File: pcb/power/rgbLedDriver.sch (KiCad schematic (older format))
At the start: 39 parts, among them Q1 Q_NPN_BCE, Q2 Q_NPN_BCE, Q3 Q_PMOS_DGS

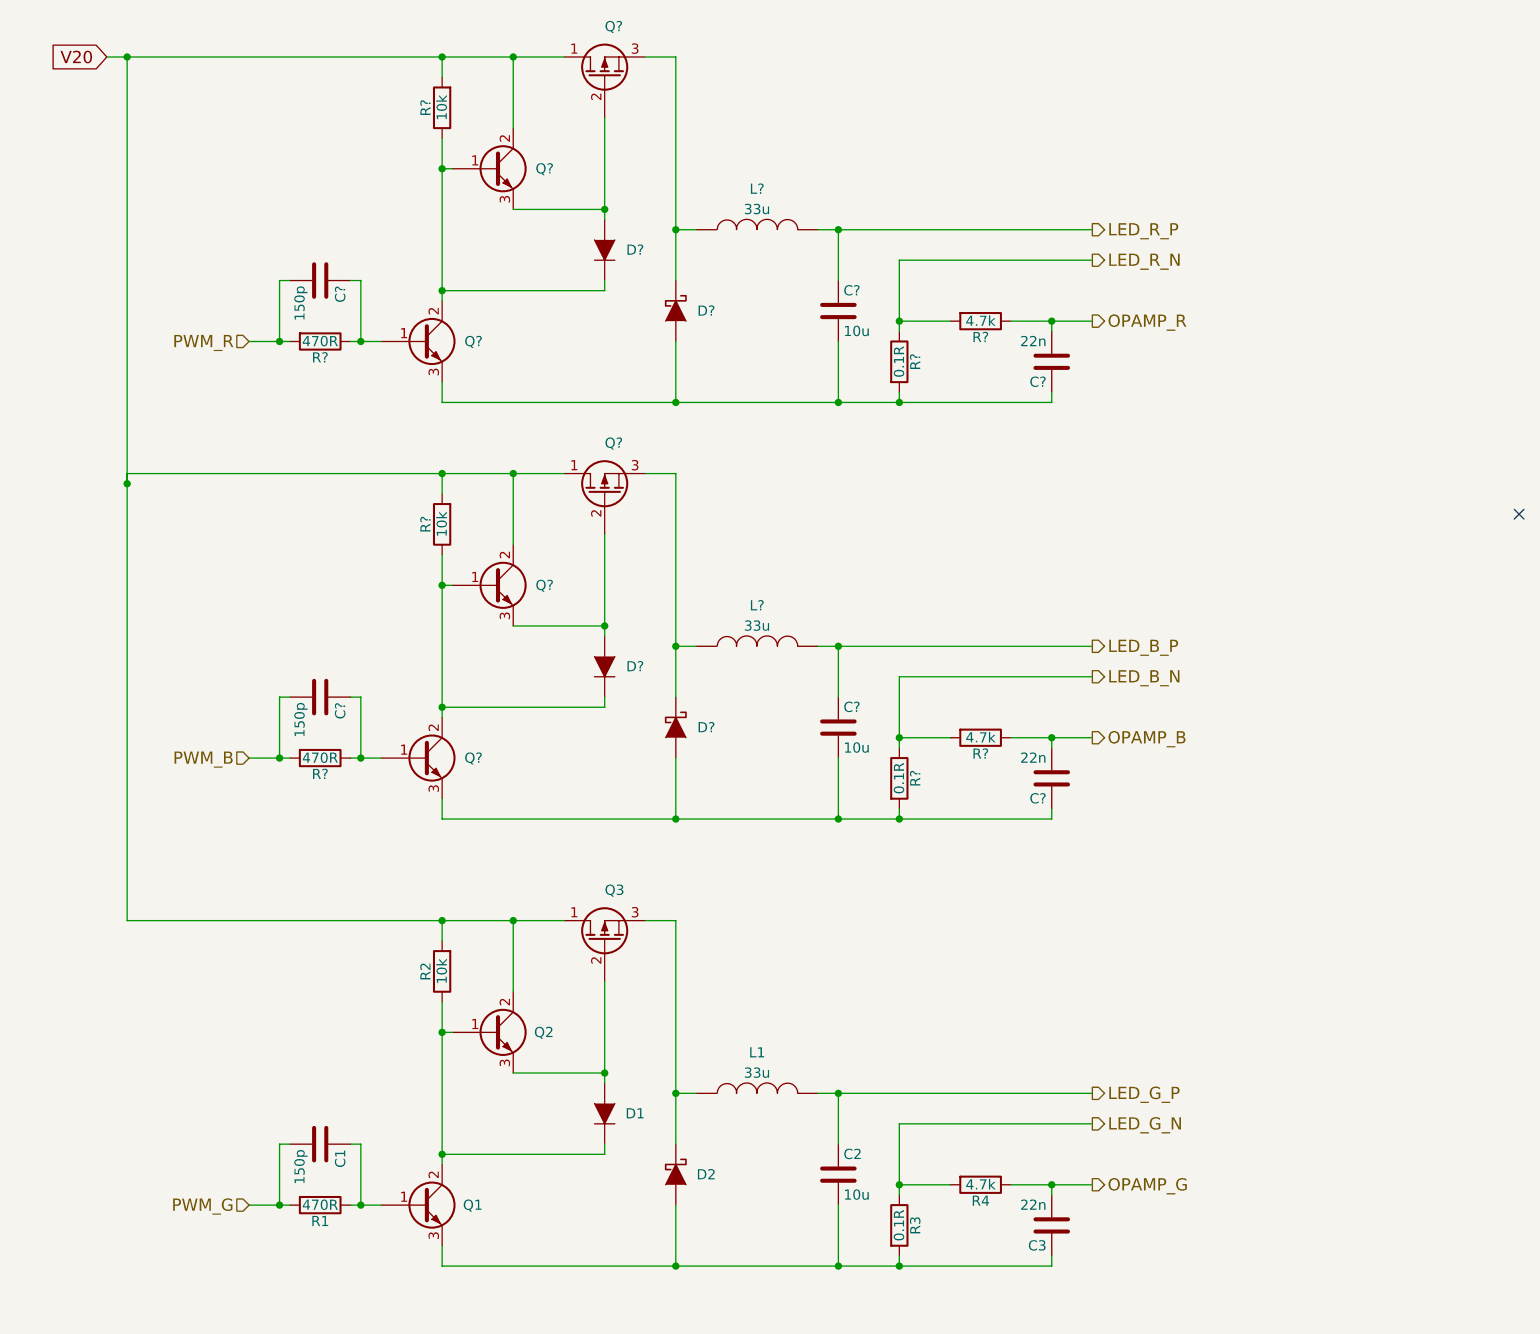
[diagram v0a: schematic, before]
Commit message: Finished LED Driver with Feedback and OLED Driver.
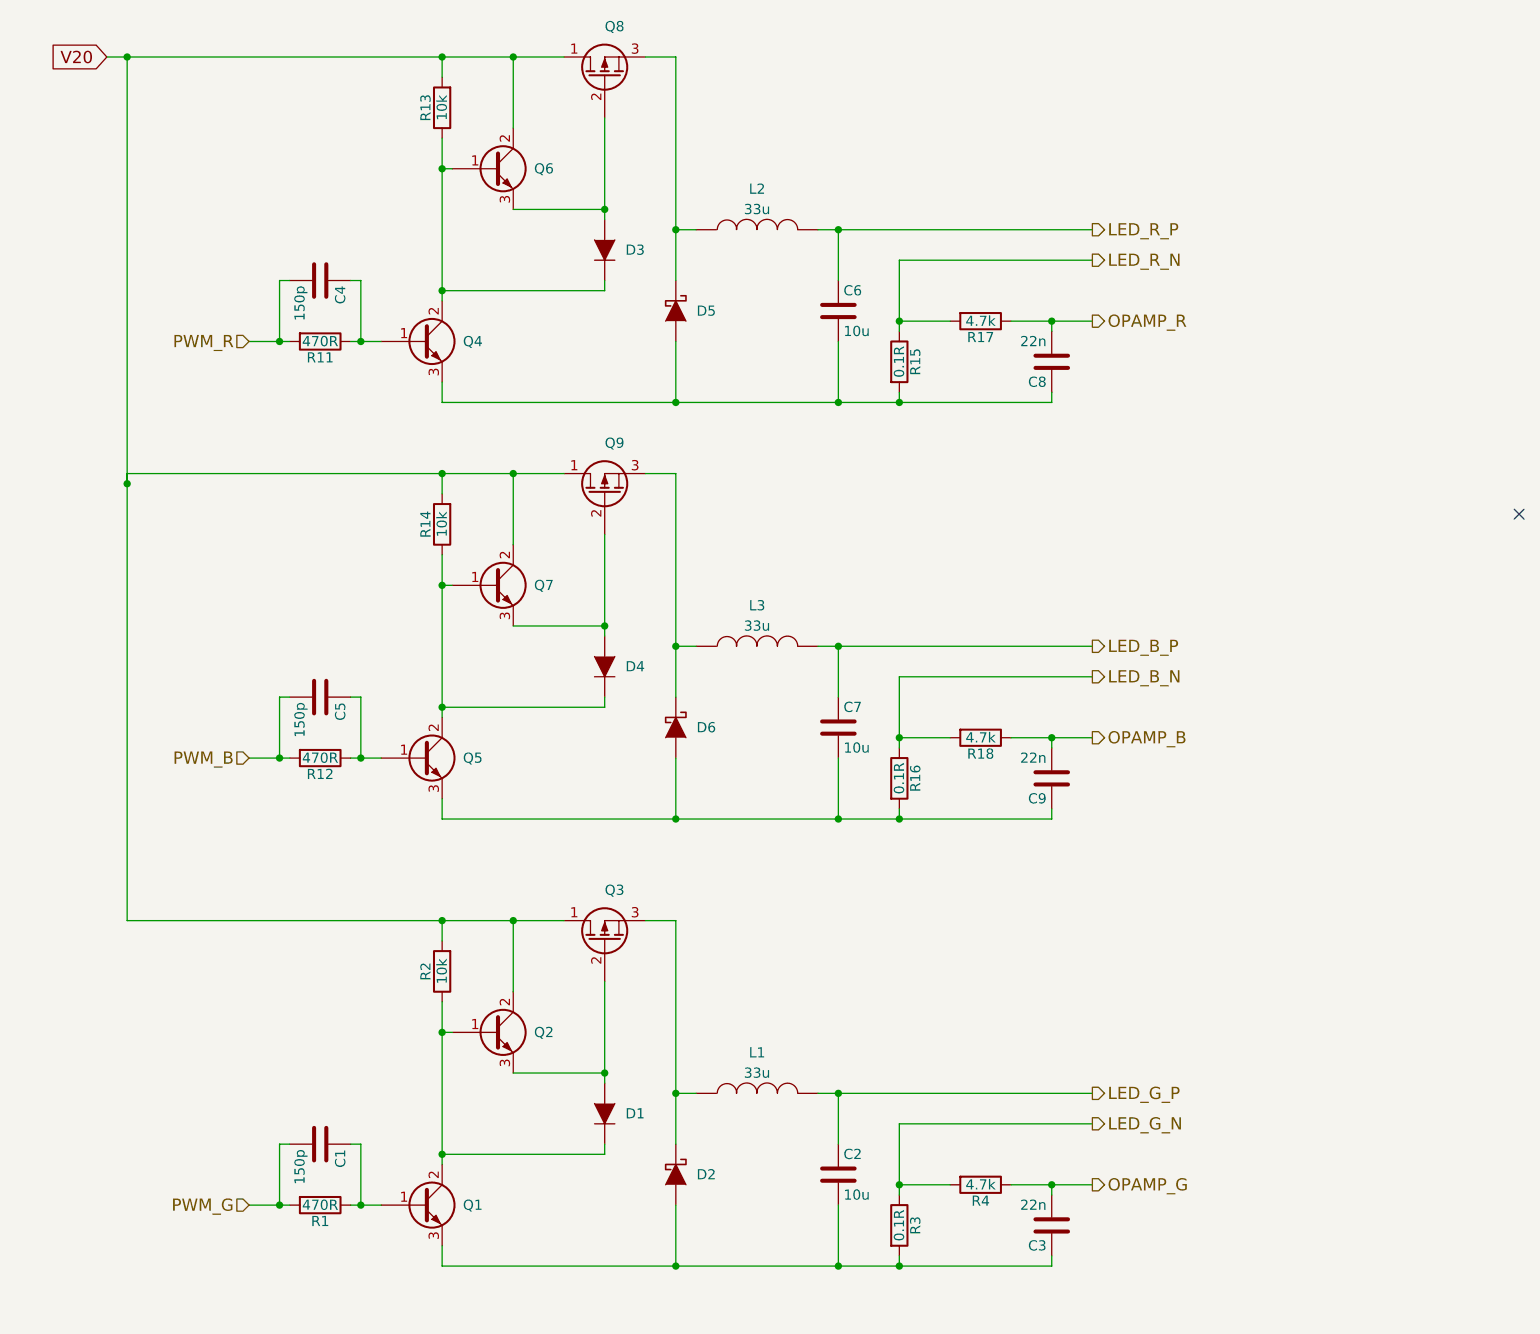
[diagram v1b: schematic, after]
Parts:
- gave numbers to parts that had none: 26
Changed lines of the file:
@@
 LIBS:contrib
 LIBS:valves
-LIBS:power-cache
+LIBS:coolLib
 EELAYER 25 0
 EELAYER END
@@
 $EndComp
 $Comp
-L Q_NPN_BCE Q?
+L Q_NPN_BCE Q7
 U 1 1 5837BEE8
 P 2850 3700
-F 0 "Q?" H 3150 3700 50  0000 R CNN
+F 0 "Q7" H 3150 3700 50  0000 R CNN
 F 1 "Q_NPN_BCE" H 3450 3650 50  0001 R CNN
 F 2 "" H 3050 3800 50  0000 C CNN
@@
 $EndComp
 $Comp
-L Q_PMOS_DGS Q?
+L Q_PMOS_DGS Q9
 U 1 1 5837BEEF
 P 3400 3250
-F 0 "Q?" V 3650 3250 50  0000 R CNN
+F 0 "Q9" V 3650 3250 50  0000 R CNN
 F 1 "Q_PMOS_DGS" H 4050 3200 50  0001 R CNN
 F 2 "" H 3600 3350 50  0000 C CNN
@@
 $EndComp
 $Comp
-L D D?
+L D D4
 U 1 1 5837BEF6
 P 3400 4100
-F 0 "D?" V 3400 3950 50  0000 C CNN
+F 0 "D4" V 3400 3950 50  0000 C CNN
 F 1 "D" H 3400 4000 50  0001 C CNN
 F 2 "" H 3400 4100 50  0000 C CNN
@@
 $EndComp
 $Comp
-L R R?
+L R R14
 U 1 1 5837BEFE
 P 2600 3400
-F 0 "R?" V 2680 3400 50  0000 C CNN
+F 0 "R14" V 2680 3400 50  0000 C CNN
 F 1 "10k" V 2600 3400 50  0000 C CNN
 F 2 "" V 2530 3400 50  0000 C CNN
@@
 $EndComp
 $Comp
-L R R?
+L R R12
 U 1 1 5837BF05
 P 2000 4550
-F 0 "R?" V 2080 4550 50  0000 C CNN
+F 0 "R12" V 2080 4550 50  0000 C CNN
 F 1 "470R" V 2000 4550 50  0000 C CNN
 F 2 "" V 1930 4550 50  0000 C CNN
@@
 $EndComp
 $Comp
-L C C?
+L C C5
 U 1 1 5837BF0C
 P 2000 4250
-F 0 "C?" H 2025 4350 50  0000 L CNN
+F 0 "C5" H 2025 4350 50  0000 L CNN
 F 1 "150p" H 2025 4150 50  0000 L CNN
 F 2 "" H 2038 4100 50  0000 C CNN
@@
 PWM_B
 $Comp
-L INDUCTOR L?
+L INDUCTOR L3
 U 1 1 5837BF14
 P 4150 4000
-F 0 "L?" V 4350 4000 50  0000 C CNN
+F 0 "L3" V 4350 4000 50  0000 C CNN
 F 1 "33u" V 4250 4000 50  0000 C CNN
 F 2 "" H 4150 4000 50  0000 C CNN
@@
 $EndComp
 $Comp
-L D_Schottky D?
+L D_Schottky D6
 U 1 1 5837BF1B
 P 3750 4400
-F 0 "D?" V 3750 4550 50  0000 C CNN
+F 0 "D6" V 3750 4550 50  0000 C CNN
 F 1 "D_Schottky" H 3750 4300 50  0001 C CNN
 F 2 "" H 3750 4400 50  0000 C CNN
@@
 $EndComp
 $Comp
-L C C?
+L C C7
 U 1 1 5837BF22
 P 4550 4400
-F 0 "C?" H 4575 4500 50  0000 L CNN
+F 0 "C7" H 4575 4500 50  0000 L CNN
 F 1 "10u" H 4575 4300 50  0000 L CNN
 F 2 "" H 4588 4250 50  0000 C CNN
@@
 LED_B_N
 $Comp
-L R R?
+L R R16
 U 1 1 5837BF2B
 P 4850 4650
-F 0 "R?" V 4930 4650 50  0000 C CNN
+F 0 "R16" V 4930 4650 50  0000 C CNN
 F 1 "0.1R" V 4850 4650 50  0000 C CNN
 F 2 "" V 4780 4650 50  0000 C CNN
@@
 $EndComp
 $Comp
-L C C?
+L C C9
 U 1 1 5837BF32
 P 5600 4650
-F 0 "C?" H 5625 4750 50  0000 L CNN
+F 0 "C9" H 5625 4750 50  0000 L CNN
 F 1 "22n" H 5625 4550 50  0000 L CNN
 F 2 "" H 5638 4500 50  0000 C CNN
@@
 $EndComp
 $Comp
-L R R?
+L R R18
 U 1 1 5837BF39
 P 5250 4450
-F 0 "R?" V 5330 4450 50  0000 C CNN
+F 0 "R18" V 5330 4450 50  0000 C CNN
 F 1 "4.7k" V 5250 4450 50  0000 C CNN
 F 2 "" V 5180 4450 50  0000 C CNN
@@
 Connection ~ 5600 4450
 $Comp
-L Q_NPN_BCE Q?
+L Q_NPN_BCE Q5
 U 1 1 5837BF6E
 P 2500 4550
-F 0 "Q?" H 2800 4550 50  0000 R CNN
+F 0 "Q5" H 2800 4550 50  0000 R CNN
 F 1 "Q_NPN_BCE" H 3100 4500 50  0001 R CNN
 F 2 "" H 2700 4650 50  0000 C CNN
@@
 $EndComp
 $Comp
-L Q_NPN_BCE Q?
+L Q_NPN_BCE Q6
 U 1 1 5837C3ED
 P 2850 1650
-F 0 "Q?" H 3150 1650 50  0000 R CNN
+F 0 "Q6" H 3150 1650 50  0000 R CNN
 F 1 "Q_NPN_BCE" H 3450 1600 50  0001 R CNN
 F 2 "" H 3050 1750 50  0000 C CNN
@@
 $EndComp
 $Comp
-L Q_PMOS_DGS Q?
+L Q_PMOS_DGS Q8
 U 1 1 5837C3F4
 P 3400 1200
-F 0 "Q?" V 3650 1200 50  0000 R CNN
+F 0 "Q8" V 3650 1200 50  0000 R CNN
 F 1 "Q_PMOS_DGS" H 4050 1150 50  0001 R CNN
 F 2 "" H 3600 1300 50  0000 C CNN
@@
 $EndComp
 $Comp
-L D D?
+L D D3
 U 1 1 5837C3FB
 P 3400 2050
-F 0 "D?" V 3400 1900 50  0000 C CNN
+F 0 "D3" V 3400 1900 50  0000 C CNN
 F 1 "D" H 3400 1950 50  0001 C CNN
 F 2 "" H 3400 2050 50  0000 C CNN
@@
 V20
 $Comp
-L R R?
+L R R13
 U 1 1 5837C403
 P 2600 1350
-F 0 "R?" V 2680 1350 50  0000 C CNN
+F 0 "R13" V 2680 1350 50  0000 C CNN
 F 1 "10k" V 2600 1350 50  0000 C CNN
 F 2 "" V 2530 1350 50  0000 C CNN
@@
 $EndComp
 $Comp
-L R R?
+L R R11
 U 1 1 5837C40A
 P 2000 2500
-F 0 "R?" V 2080 2500 50  0000 C CNN
+F 0 "R11" V 2080 2500 50  0000 C CNN
 F 1 "470R" V 2000 2500 50  0000 C CNN
 F 2 "" V 1930 2500 50  0000 C CNN
@@
 $EndComp
 $Comp
-L C C?
+L C C4
 U 1 1 5837C411
 P 2000 2200
-F 0 "C?" H 2025 2300 50  0000 L CNN
+F 0 "C4" H 2025 2300 50  0000 L CNN
 F 1 "150p" H 2025 2100 50  0000 L CNN
 F 2 "" H 2038 2050 50  0000 C CNN
@@
 PWM_R
 $Comp
-L INDUCTOR L?
+L INDUCTOR L2
 U 1 1 5837C419
 P 4150 1950
-F 0 "L?" V 4350 1950 50  0000 C CNN
+F 0 "L2" V 4350 1950 50  0000 C CNN
 F 1 "33u" V 4250 1950 50  0000 C CNN
 F 2 "" H 4150 1950 50  0000 C CNN
@@
 $EndComp
 $Comp
-L D_Schottky D?
+L D_Schottky D5
 U 1 1 5837C420
 P 3750 2350
-F 0 "D?" V 3750 2500 50  0000 C CNN
+F 0 "D5" V 3750 2500 50  0000 C CNN
 F 1 "D_Schottky" H 3750 2250 50  0001 C CNN
 F 2 "" H 3750 2350 50  0000 C CNN
@@
 $EndComp
 $Comp
-L C C?
+L C C6
 U 1 1 5837C427
 P 4550 2350
-F 0 "C?" H 4575 2450 50  0000 L CNN
+F 0 "C6" H 4575 2450 50  0000 L CNN
 F 1 "10u" H 4575 2250 50  0000 L CNN
 F 2 "" H 4588 2200 50  0000 C CNN
@@
 LED_R_N
 $Comp
-L R R?
+L R R15
 U 1 1 5837C430
 P 4850 2600
-F 0 "R?" V 4930 2600 50  0000 C CNN
+F 0 "R15" V 4930 2600 50  0000 C CNN
 F 1 "0.1R" V 4850 2600 50  0000 C CNN
 F 2 "" V 4780 2600 50  0000 C CNN
@@
 $EndComp
 $Comp
-L C C?
+L C C8
 U 1 1 5837C437
 P 5600 2600
-F 0 "C?" H 5625 2700 50  0000 L CNN
+F 0 "C8" H 5625 2700 50  0000 L CNN
 F 1 "22n" H 5625 2500 50  0000 L CNN
 F 2 "" H 5638 2450 50  0000 C CNN
@@
 $EndComp
 $Comp
-L R R?
+L R R17
 U 1 1 5837C43E
 P 5250 2400
-F 0 "R?" V 5330 2400 50  0000 C CNN
+F 0 "R17" V 5330 2400 50  0000 C CNN
 F 1 "4.7k" V 5250 2400 50  0000 C CNN
 F 2 "" V 5180 2400 50  0000 C CNN
@@
 Connection ~ 5600 2400
 $Comp
-L Q_NPN_BCE Q?
+L Q_NPN_BCE Q4
 U 1 1 5837C473
 P 2500 2500
-F 0 "Q?" H 2800 2500 50  0000 R CNN
+F 0 "Q4" H 2800 2500 50  0000 R CNN
 F 1 "Q_NPN_BCE" H 3100 2450 50  0001 R CNN
 F 2 "" H 2700 2600 50  0000 C CNN

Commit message: Finished driver for 2.8 V.
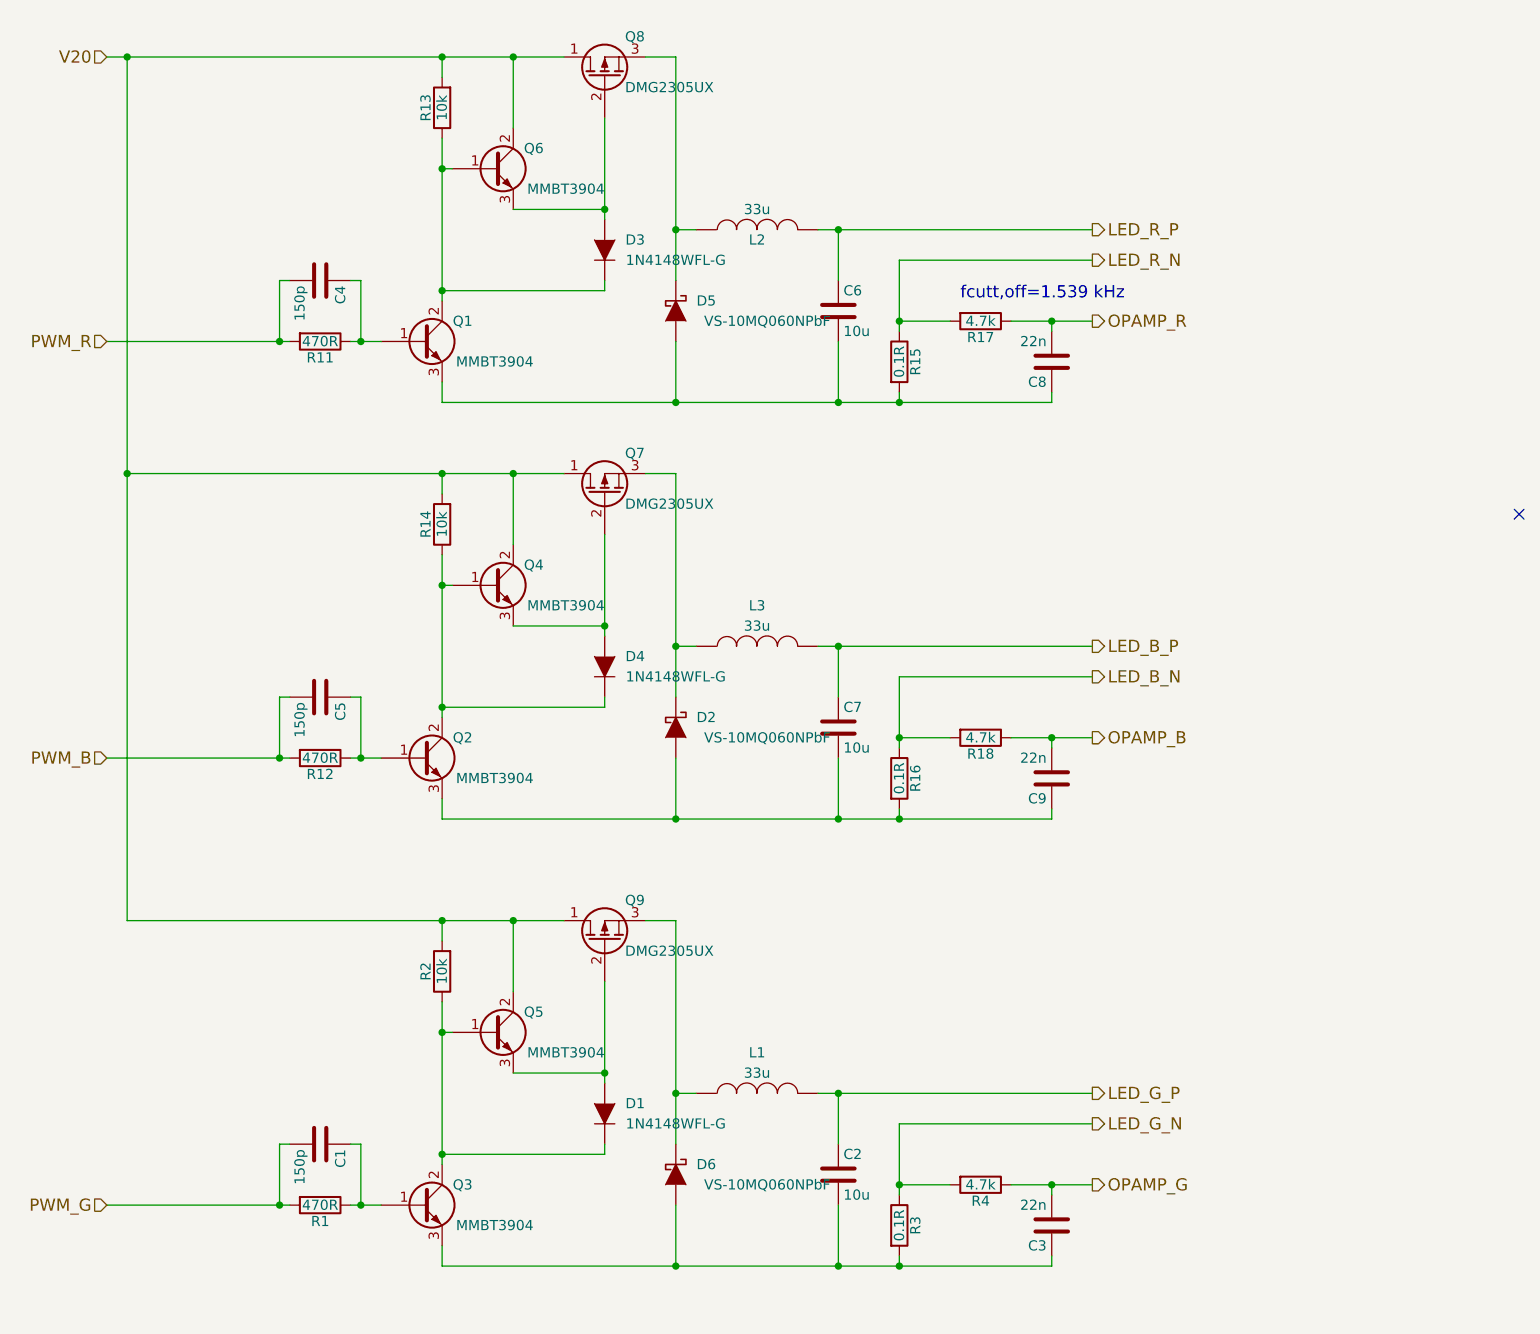
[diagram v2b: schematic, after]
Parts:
- removed Q3: Q_PMOS_DGS, symbol Q_PMOS_DGS
- removed Q7: Q_NPN_BCE, symbol Q_NPN_BCE
- added Q3: MMBT3904, symbol Q_NPN_BCE
- added Q7: DMG2305UX, symbol Q_PMOS_DGS
- D1, D3, D4: value D -> 1N4148WFL-G
- D2, D5, D6: value D_Schottky -> VS-10MQ060NPbF
- Q1, Q2, Q4, Q5, Q6: value Q_NPN_BCE -> MMBT3904
- Q8, Q9: value Q_PMOS_DGS -> DMG2305UX
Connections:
- net V20: now also Q4.2 (C), Q5.2 (C), Q7.1 (D); no longer Q2.2 (C)
- net at D1.1 (K), R2.1: now also Q5.1 (B), Q3.2 (C); no longer Q1.2 (C), Q2.1 (B)
- net at D1.2 (A): now also Q5.3 (E), Q9.2 (G); no longer Q2.3 (E)
- net at L1.1: now also D6.1 (K), Q9.3 (S); no longer D2.1 (K)
- net at C1.1, R1.1: now also Q3.1 (B); no longer Q1.1 (B)
- net at C2.2, C3.1, R3.2: now also D6.2 (A), Q3.3 (E); no longer D2.2 (A), Q1.3 (E)
- net at D4.1 (K), R14.1: now also Q2.2 (C), Q4.1 (B); no longer Q5.2 (C)
- net at D4.2 (A): now also Q4.3 (E), Q7.2 (G); no longer Q9.2 (G)
- net at C5.1, R12.1: now also Q2.1 (B); no longer Q5.1 (B)
- net at C7.2, C9.1, R16.2: now also D2.2 (A), Q2.3 (E); no longer D6.2 (A), Q5.3 (E)
- net at D3.1 (K), Q6.1 (B), R13.1: now also Q1.2 (C); no longer Q4.2 (C)
- net at C4.1, R11.1: now also Q1.1 (B); no longer Q4.1 (B)
- net at C6.2, C8.1, D5.2 (A)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: now also Q1.3 (E); no longer Q4.3 (E)
- new net: D2.1 (K), L3.1, Q7.3 (S)
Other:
- note added: "fcutt,off=1.539 kHz"
